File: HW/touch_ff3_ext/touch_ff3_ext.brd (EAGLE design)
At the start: 42 x 27.5 mm, 6 parts, among them M1 SMALL_SERVO, P8 DF9-31P, Q1 MOSFET-NCHANNELAO3404A, X3 DF9-31S

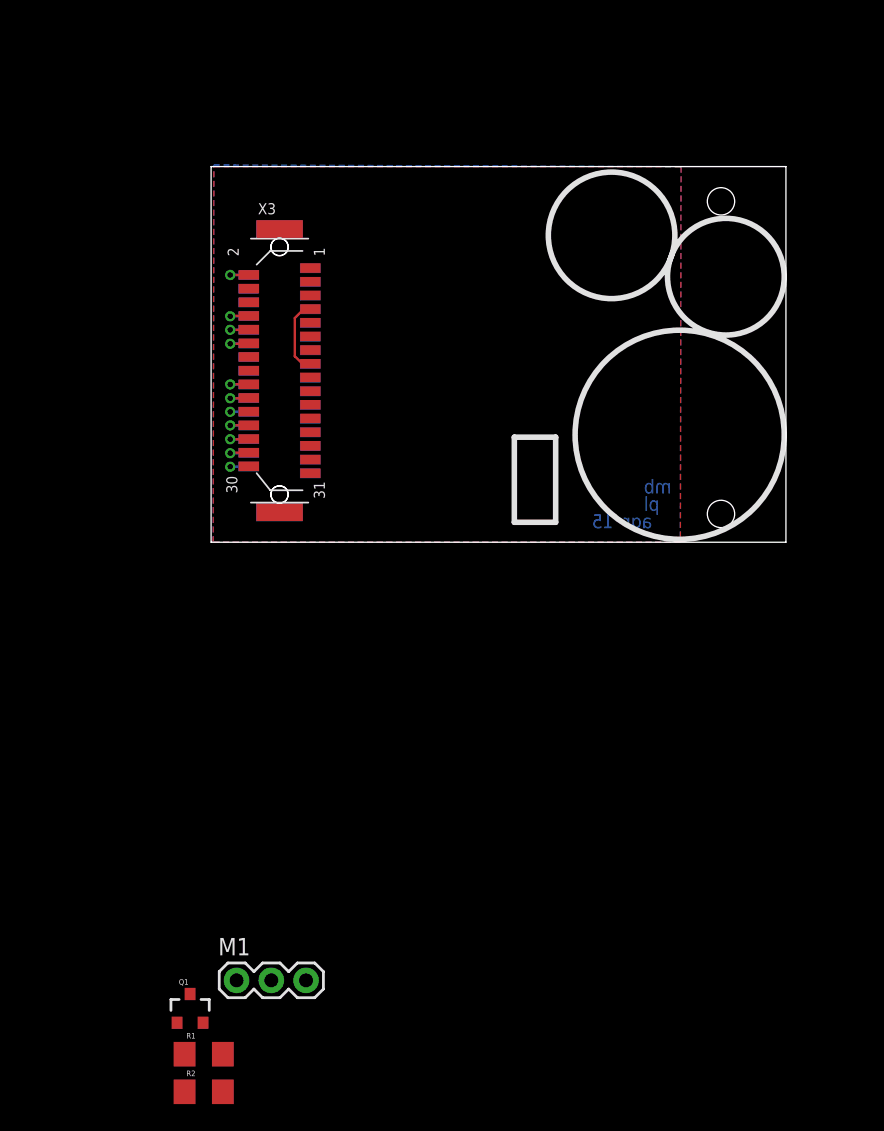
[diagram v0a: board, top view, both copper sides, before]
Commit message: updated pcb, removed .swp file from fw dir
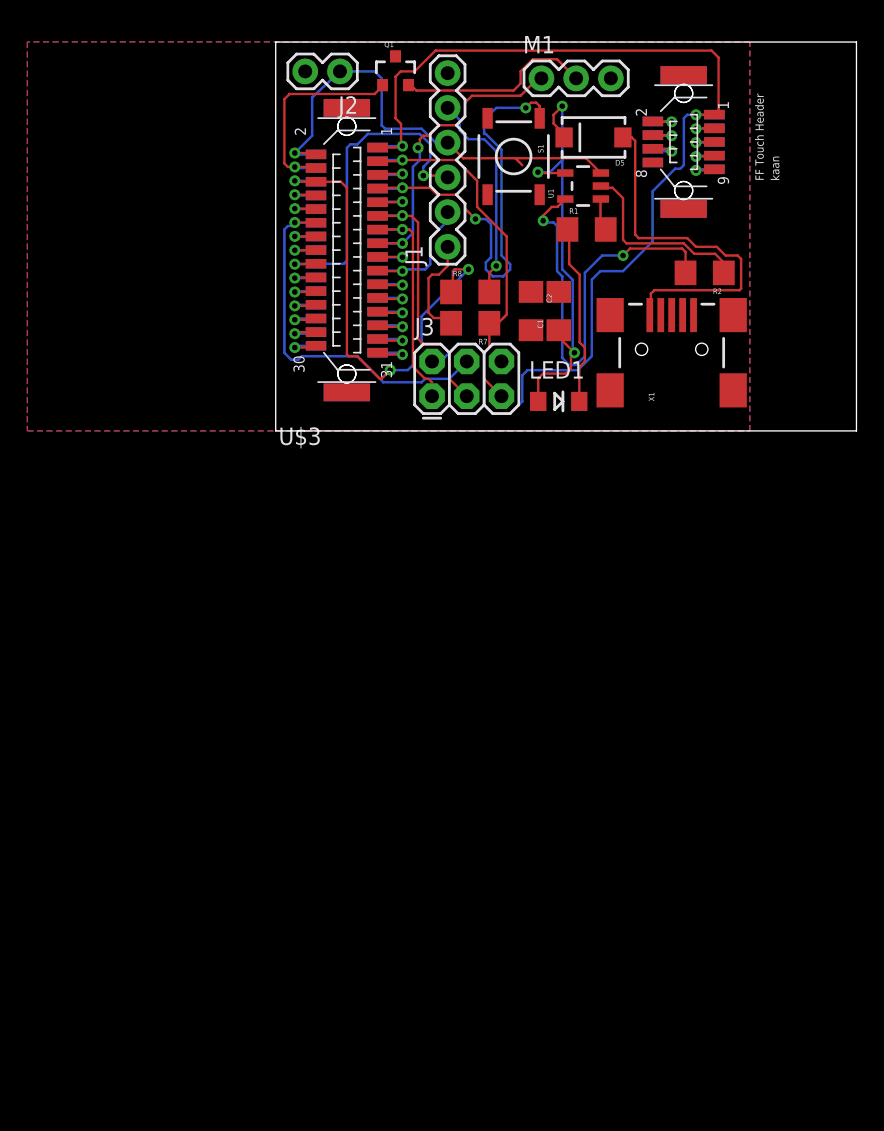
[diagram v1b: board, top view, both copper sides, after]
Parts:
- removed P8: DF9-31P, con-hirose:DF9-31P
- removed X3: DF9-31S, con-hirose:DF9-31S
- added C1, C2: 4.7 uF, SparkFun-Capacitors:1206
- added D5: MBRA140, SparkFun-DiscreteSemi:SMA-DIODE
- added J1: (no value), SparkFun-Connectors:1X06
- added J2: (no value), SparkFun-Connectors:1X02
- added J3: AVR_SPI_PRG_6PTH, SparkFun-Connectors:2X3
- added LED1: (no value), LilyPad-Wearables:LED-1206
- added R7, R8: 0, SparkFun-Passives:1206
- added S1: SWITCH-MOMENTARY-2SMD, SparkFun-Electromechanical:TACTILE-SWITCH-SMD
- added U$2: FIREFLY_MICRO_MATE, Boards:FIREFLY_MICRO_MATE
- added U$3: FIREFLY_MICRO_BOARD, Boards:FIREFLY_MICRO_BOARD
- added U1: MCP73831, SparkFun-PowerIC:SOT23-5
- added X1: USBSMD, SparkFun-Connectors:USB-MINIB
- Q1: value MOSFET-NCHANNELAO3404A -> MOSFET-PCHANNEL
- R1: value 10K -> 330; device SparkFun-Passives:1206 -> SparkFun-Resistors:1206
- R2: value 10K -> 2K; device SparkFun-Passives:1206 -> SparkFun-Resistors:1206
- moved R2 70.2 mm to (55.9, 29.1), turned to 180 degrees
- moved Q1 70.2 mm to (33.3, 43.8)
- moved M1 69.6 mm to (43.9, 43.3)
- moved R1 66.5 mm to (47.2, 32.3)
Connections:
- removed net HPB4: M1.1, R2.2
- removed net PD0: X3.6
- new net N$10: D5.A, X1.VBUS
- new net N$17: R2.2, U1.5
- new net N$18: J1.1, R7.2
- new net N$19: J1.5, R8.2
- new net N$6: C1.1, D5.C, LED1.A, U1.4
- new net N$7: R1.2, U1.1
- new net N$9: LED1.C, R1.1
- new net POT_3: U$2.S3, U$3.P3
- new net POT_5: U$2.S5, U$3.P5
- new net POT_7: U$2.S7, U$3.P7
- new net POT_9: U$2.S9, U$3.P9
- new net POT_CS: U$2.S6, U$3.P6
- new net POT_OUT: U$2.S2, U$3.P2
- new net POT_UD: U$2.S4, U$3.P4
- net AREF: now also U$2.22, U$3.22; no longer P8.22, X3.22
- net GND: now also C1.2, C2.2, J1.6, J2.2, J3.6, S1.3, U$2.31, U$2.S8, U$3.31, U$3.P8, X1.GND; no longer P8.31, X3.31
- net MISO: now also J3.1, U$2.13, U$3.13; no longer P8.13, X3.13
- net MOSI: now also J3.4, U$2.12, U$3.12; no longer P8.12, X3.12
- net N$1: now also U1.2; no longer Q1.3
- net N$2: now also M1.2; no longer Q1.1, R1.1
- net PB4: now also U$2.14, U$3.14; no longer P8.14, R1.2, X3.14
- net PB5: now also M1.1, U$2.15, U$3.15; no longer P8.15, X3.15
- net PB6: now also U$2.16, U$3.16; no longer P8.16, X3.16
- net PB7: now also U$2.17, U$3.17; no longer P8.17, X3.17
- net PD1: now also S1.1, U$2.7, U$3.7; no longer P8.7, X3.7
- net PE2: now also U$2.20, U$3.20; no longer P8.20, X3.20
- net PE3: now also U$2.21, U$3.21; no longer P8.21, X3.21
- net PG0: now also Q1.1, U$2.4, U$3.4; no longer P8.4, X3.4
- net PG1: now also U$2.5, U$3.5; no longer P8.5, X3.5
- net PORTF0: now also U$2.23, U$3.23; no longer P8.23, X3.23
- net PORTF1: now also U$2.24, U$3.24; no longer P8.24, X3.24
- net PORTF2: now also U$2.25, U$3.25; no longer P8.25, X3.25
- net PORTF3: now also U$2.26, U$3.26; no longer P8.26, X3.26
- net PORTF4: now also U$2.27, U$3.27; no longer P8.27, X3.27
- net PORTF5: now also U$2.28, U$3.28; no longer P8.28, X3.28
- net PORTF6: now also U$2.29, U$3.29; no longer P8.29, X3.29
- net PORTF7: now also U$2.30, U$3.30; no longer P8.30
- net RST: now also J3.5, R7.1, U$2.3, U$3.3; no longer P8.3, X3.3
- net RX0_MCU: now also J1.3, U$2.18, U$3.18; no longer P8.18, X3.18
- net RX1_MCU: now also U$2.8, U$3.8; no longer P8.8, X3.8
- net SCK: now also J3.3, U$2.11, U$3.11; no longer P8.11, X3.11
- net SCL: now also R8.1, U$2.6, U$3.6; no longer P8.6
- net SSN: now also U$2.10, U$3.10; no longer P8.10, X3.10
- net TX0_MCU: now also J1.2, U$2.19, U$3.19; no longer P8.19, X3.19
- net TX1_MCU: now also U$2.9, U$3.9; no longer P8.9, X3.9
- net VDD: now also J3.2, U$2.1, U$2.S1, U$3.1, U$3.P1; no longer P8.1, X3.1
- net V_UNREG: now also C2.1, J1.4, J2.1, Q1.3, U$2.2, U$3.2, U1.3; no longer M1.2, P8.2, X3.2
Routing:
- net VDD: track 0.00 -> 82.5 mm, vias 0 -> 2
- net SCL: track 0.00 -> 35.7 mm, vias 0 -> 3
- net PD1: track 0.00 -> 34.7 mm, vias 0 -> 3
- net N$6: track 0.00 -> 33.3 mm, vias 0 -> 3
- net V_UNREG: track 2.75 -> 35.4 mm
- net N$17: track 0.00 -> 31.6 mm, vias 0 -> 2
- net RST: track 0.00 -> 28.0 mm, vias 0 -> 1
- net N$10: track 0.00 -> 26.9 mm
- net MOSI: track 2.74 -> 28.2 mm
- net RX0_MCU: track 2.72 -> 24.9 mm, vias 1 -> 2
- net SCK: track 0.00 -> 19.9 mm, vias 0 -> 1
- net PB5: track 5.09 -> 23.2 mm, vias 0 -> 2
- net MISO: track 0.00 -> 17.2 mm, vias 0 -> 1
- net PG0: track 0.00 -> 16.4 mm, vias 0 -> 1
- net N$19: track 0.00 -> 15.8 mm, vias 0 -> 1
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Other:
- board size 42 x 27.5 mm -> 42.5 x 28.4 mm
- board text added: "FF Touch Header"
- board text added: "kaan"
- board text removed: "agr '15"
- board text removed: "mb"
- board text removed: "pl"

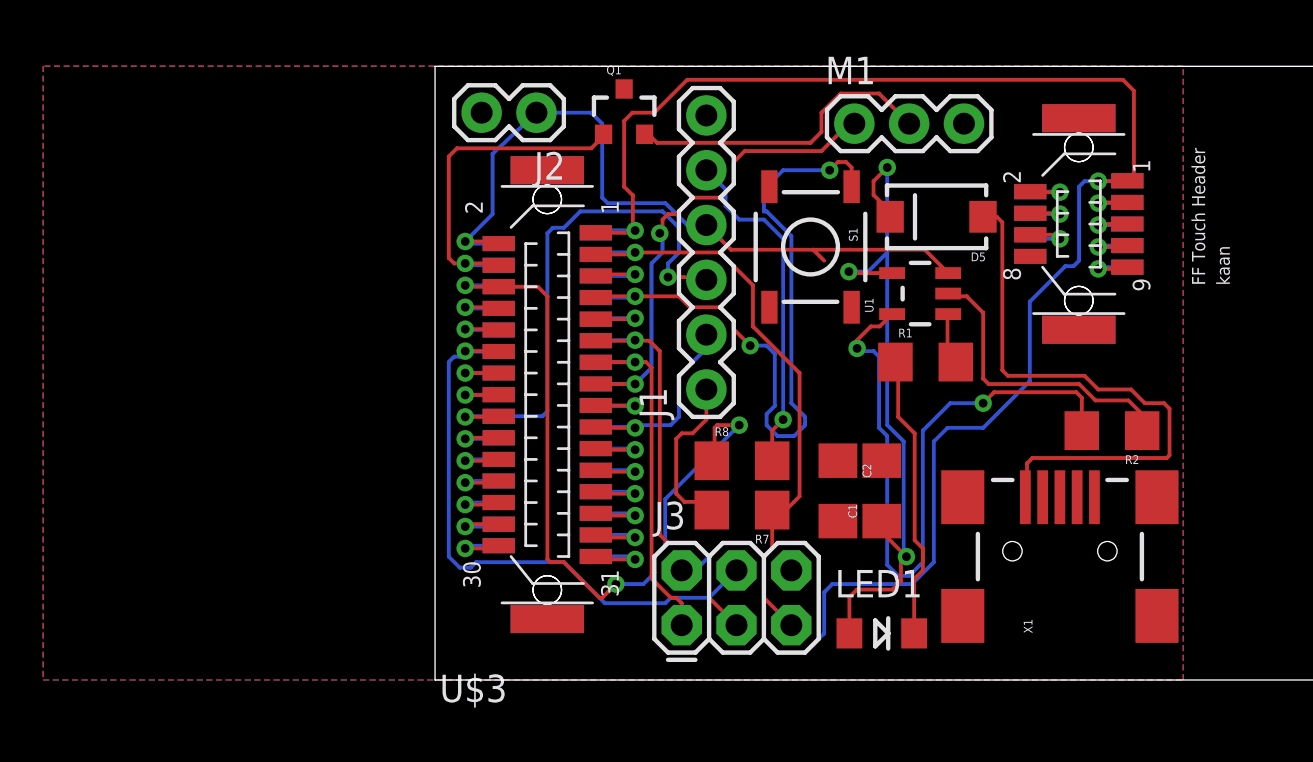
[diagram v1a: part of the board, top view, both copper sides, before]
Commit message: updated transistor, routed 1 last connection, added vias to balance out gnd planes
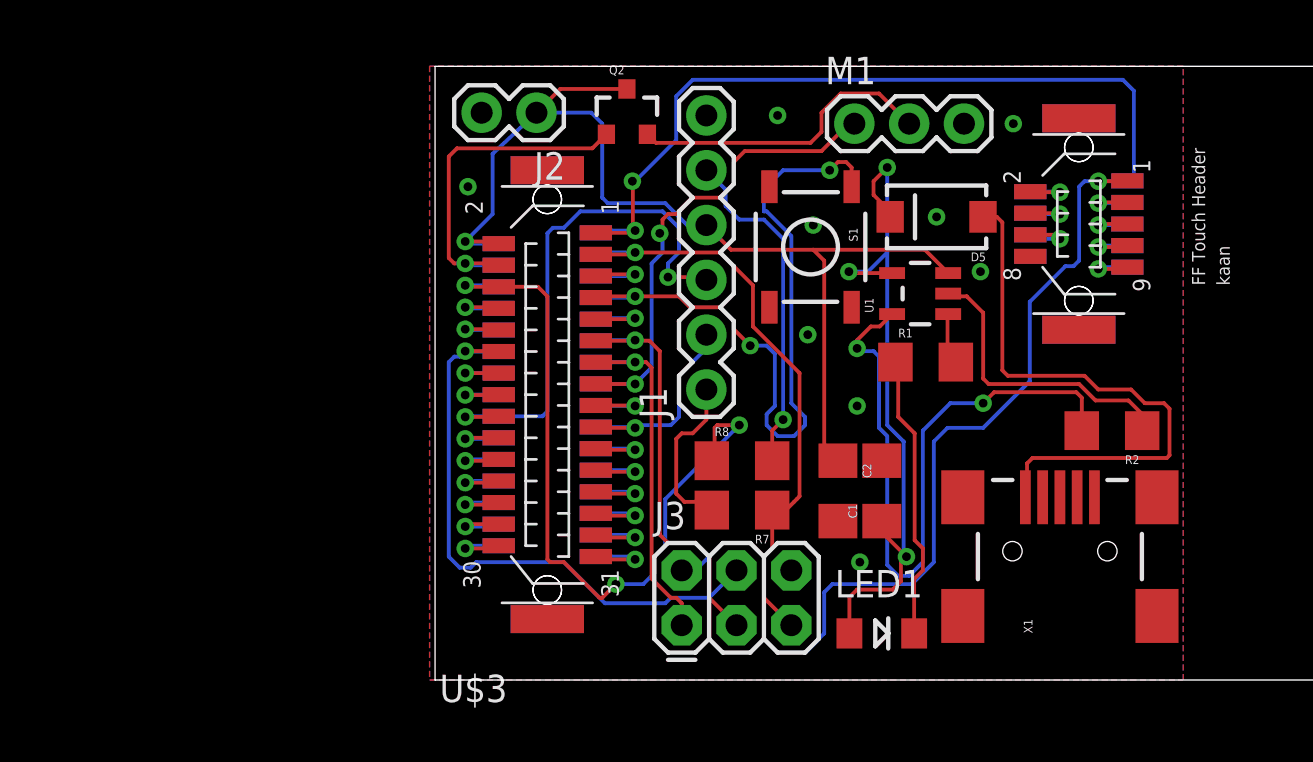
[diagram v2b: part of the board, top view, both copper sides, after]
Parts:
- removed Q1: MOSFET-PCHANNEL, SparkFun-DiscreteSemi:SOT23-3
- added Q2: MOSFET-PCHANNEL, SparkFun-DiscreteSemi:SOT23-3
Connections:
- net N$2: now also Q2.2; no longer Q1.2
- net PG0: now also Q2.1; no longer Q1.1
- net V_UNREG: now also Q2.3; no longer Q1.3
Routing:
- net V_UNREG: track 35.4 -> 49.6 mm
- net VDD: track 82.5 -> 81.5 mm, vias 2 -> 3
- net GND: vias 1 -> 10
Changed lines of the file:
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@@
 <element name="R1" library="SparkFun-Resistors" package="1206" value="330" x="47.244" y="32.258"/>
 <element name="R2" library="SparkFun-Resistors" package="1206" value="2K" x="55.88" y="29.083" rot="R180"/>
-<element name="Q1" library="SparkFun-DiscreteSemi" package="SOT23-3" value="MOSFET-PCHANNEL" x="33.274" y="43.815">
-<attribute name="PROD_ID" value="TRANS-08285" x="33.274" y="43.815" size="1.778" layer="27" display="off"/>
+<element name="Q2" library="SparkFun-DiscreteSemi" package="SOT23-3" value="MOSFET-PCHANNEL" x="33.401" y="43.815">
+<attribute name="PROD_ID" value="TRANS-08285" x="33.401" y="43.815" size="1.778" layer="27" display="off"/>
 </element>
 </elements>
@@
 <wire x1="32.0964" y1="23.114" x2="31.9616" y2="23.2488" width="0.1778" layer="1"/>
 <polygon width="0.1778" layer="1">
-<vertex x="6.35" y="45.974"/>
-<vertex x="6.35" y="17.526"/>
+<vertex x="24.257" y="45.974"/>
+<vertex x="24.257" y="17.526"/>
 <vertex x="59.182" y="17.526"/>
 <vertex x="59.182" y="45.974"/>
 </polygon>
 <polygon width="0.1778" layer="16">
-<vertex x="6.35" y="45.974"/>
-<vertex x="6.35" y="17.526"/>
+<vertex x="24.257" y="45.974"/>
+<vertex x="24.257" y="17.526"/>
 <vertex x="59.182" y="17.526"/>
 <vertex x="59.182" y="45.974"/>
@@
 <contactref element="C1" pad="2"/>
 <contactref element="C2" pad="2"/>
+<via x="49.784" y="36.449" extent="1-16" drill="0.4064" diameter="0.508"/>
+<via x="47.752" y="38.989" extent="1-16" drill="0.4064" diameter="0.508"/>
+<via x="51.308" y="43.307" extent="1-16" drill="0.4064" diameter="0.508"/>
+<via x="40.386" y="43.688" extent="1-16" drill="0.4064" diameter="0.508"/>
+<via x="42.037" y="38.608" extent="1-16" drill="0.4064" diameter="0.508"/>
+<via x="26.035" y="40.386" extent="1-16" drill="0.4064" diameter="0.508"/>
+<via x="41.783" y="33.528" extent="1-16" drill="0.4064" diameter="0.508"/>
+<via x="44.069" y="30.226" extent="1-16" drill="0.4064" diameter="0.508"/>
+<via x="44.196" y="22.987" extent="1-16" drill="0.4064" diameter="0.508"/>
 </signal>
 <signal name="VDD">
@@
 <wire x1="33.782" y1="38.354" x2="32.0688" y2="38.354" width="0.1778" layer="16"/>
 <wire x1="32.0688" y1="38.354" x2="31.9616" y2="38.2468" width="0.1778" layer="16"/>
-<wire x1="33.6768" y1="38.2488" x2="33.6768" y2="39.9832" width="0.1778" layer="1"/>
-<wire x1="33.6768" y1="39.9832" x2="33.274" y2="40.386" width="0.1778" layer="1"/>
-<wire x1="33.274" y1="40.386" x2="33.274" y2="43.434" width="0.1778" layer="1"/>
-<wire x1="33.274" y1="43.434" x2="33.655" y2="43.815" width="0.1778" layer="1"/>
-<wire x1="33.655" y1="43.815" x2="34.671" y2="43.815" width="0.1778" layer="1"/>
-<wire x1="34.671" y1="43.815" x2="36.195" y2="45.339" width="0.1778" layer="1"/>
-<wire x1="36.195" y1="45.339" x2="56.388" y2="45.339" width="0.1778" layer="1"/>
-<wire x1="56.388" y1="45.339" x2="56.896" y2="44.831" width="0.1778" layer="1"/>
-<wire x1="56.896" y1="44.831" x2="56.896" y2="40.9588" width="0.1778" layer="1"/>
-<wire x1="56.896" y1="40.9588" x2="56.594" y2="40.6568" width="0.1778" layer="1"/>
+<wire x1="33.6768" y1="38.2488" x2="33.6768" y2="40.6182" width="0.1778" layer="1"/>
+<wire x1="33.6768" y1="40.6182" x2="33.655" y2="40.64" width="0.1778" layer="1"/>
+<via x="33.655" y="40.64" extent="1-16" drill="0.4064" diameter="0.508"/>
+<wire x1="33.655" y1="40.64" x2="33.782" y2="40.64" width="0.1778" layer="16"/>
+<wire x1="33.782" y1="40.64" x2="35.687" y2="42.545" width="0.1778" layer="16"/>
+<wire x1="35.687" y1="42.545" x2="35.687" y2="44.577" width="0.1778" layer="16"/>
+<wire x1="35.687" y1="44.577" x2="36.449" y2="45.339" width="0.1778" layer="16"/>
+<wire x1="36.449" y1="45.339" x2="56.388" y2="45.339" width="0.1778" layer="16"/>
+<wire x1="56.388" y1="45.339" x2="56.896" y2="44.831" width="0.1778" layer="16"/>
+<wire x1="56.896" y1="44.831" x2="56.896" y2="40.9568" width="0.1778" layer="16"/>
+<wire x1="56.896" y1="40.9568" x2="56.594" y2="40.6548" width="0.1778" layer="16"/>
 </signal>
 <signal name="SSN">
@@
 <wire x1="47.2081" y1="37.465" x2="48.2901" y2="36.383" width="0.1778" layer="1"/>
 <wire x1="42.545" y1="36.957" x2="42.037" y2="37.465" width="0.1778" layer="1"/>
-<contactref element="Q1" pad="3"/>
 <wire x1="25.908" y1="37.846" x2="27.178" y2="39.116" width="0.1778" layer="16"/>
 <wire x1="27.178" y1="39.116" x2="27.178" y2="41.91" width="0.1778" layer="16"/>
@@
 <wire x1="32.258" y1="43.307" x2="31.75" y2="43.815" width="0.1778" layer="16"/>
 <wire x1="31.75" y1="43.815" x2="29.21" y2="43.815" width="0.1778" layer="16"/>
-<wire x1="31.75" y1="43.815" x2="33.274" y2="44.915" width="0" layer="19" extent="1-16"/>
-<wire x1="43.18" y1="27.689" x2="42.545" y2="36.957" width="0" layer="19" extent="1-1"/>
+<contactref element="Q2" pad="3"/>
+<wire x1="33.401" y1="44.915" x2="30.31" y2="44.915" width="0.1778" layer="1"/>
+<wire x1="30.31" y1="44.915" x2="29.21" y2="43.815" width="0.1778" layer="1"/>
+<wire x1="42.545" y1="36.957" x2="42.545" y2="28.324" width="0.1778" layer="1"/>
+<wire x1="42.545" y1="28.324" x2="43.18" y2="27.689" width="0.1778" layer="1"/>
 </signal>
 <signal name="PG0">
 <contactref element="U$2" pad="4"/>
 <contactref element="U$3" pad="4"/>
-<contactref element="Q1" pad="1"/>
 <wire x1="27.4616" y1="36.7468" x2="25.9912" y2="36.7468" width="0.1778" layer="16"/>
 <wire x1="25.9912" y1="36.7468" x2="25.908" y2="36.83" width="0.1778" layer="16"/>
@@
 <wire x1="25.908" y1="36.83" x2="27.3804" y2="36.83" width="0.1778" layer="1"/>
 <wire x1="27.3804" y1="36.83" x2="27.4616" y2="36.7488" width="0.1778" layer="1"/>
-<wire x1="32.324" y1="42.815" x2="32.324" y2="42.738" width="0.1778" layer="1"/>
-<wire x1="32.324" y1="42.738" x2="31.75" y2="42.164" width="0.1778" layer="1"/>
-<wire x1="31.75" y1="42.164" x2="25.527" y2="42.164" width="0.1778" layer="1"/>
+<wire x1="31.8" y1="42.164" x2="25.527" y2="42.164" width="0.1778" layer="1"/>
 <wire x1="25.527" y1="42.164" x2="25.146" y2="41.783" width="0.1778" layer="1"/>
 <wire x1="25.146" y1="41.783" x2="25.146" y2="37.084" width="0.1778" layer="1"/>
 <wire x1="25.146" y1="37.084" x2="25.4" y2="36.83" width="0.1778" layer="1"/>
 <wire x1="25.4" y1="36.83" x2="25.908" y2="36.83" width="0.1778" layer="1"/>
+<contactref element="Q2" pad="1"/>
+<wire x1="31.8" y1="42.164" x2="32.451" y2="42.815" width="0.1778" layer="1"/>
 </signal>
 <signal name="PG1">
@@
 </signal>
 <signal name="N$2">
-<contactref element="Q1" pad="2"/>
 <contactref element="M1" pad="2"/>
-<wire x1="34.224" y1="42.815" x2="34.401" y2="42.815" width="0.1778" layer="1"/>
-<wire x1="34.401" y1="42.815" x2="34.798" y2="42.418" width="0.1778" layer="1"/>
-<wire x1="34.798" y1="42.418" x2="41.91" y2="42.418" width="0.1778" layer="1"/>
+<wire x1="34.748" y1="42.418" x2="41.91" y2="42.418" width="0.1778" layer="1"/>
 <wire x1="41.91" y1="42.418" x2="42.418" y2="42.926" width="0.1778" layer="1"/>
 <wire x1="42.418" y1="42.926" x2="42.418" y2="43.815" width="0.1778" layer="1"/>
@@
 <wire x1="43.307" y1="44.704" x2="45.085" y2="44.704" width="0.1778" layer="1"/>
 <wire x1="45.085" y1="44.704" x2="46.482" y2="43.307" width="0.1778" layer="1"/>
+<contactref element="Q2" pad="2"/>
+<wire x1="34.748" y1="42.418" x2="34.351" y2="42.815" width="0.1778" layer="1"/>
 </signal>
 </signals>
